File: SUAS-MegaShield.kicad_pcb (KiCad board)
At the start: 2 copper layers, 102.1 x 53.8 mm, 2 parts

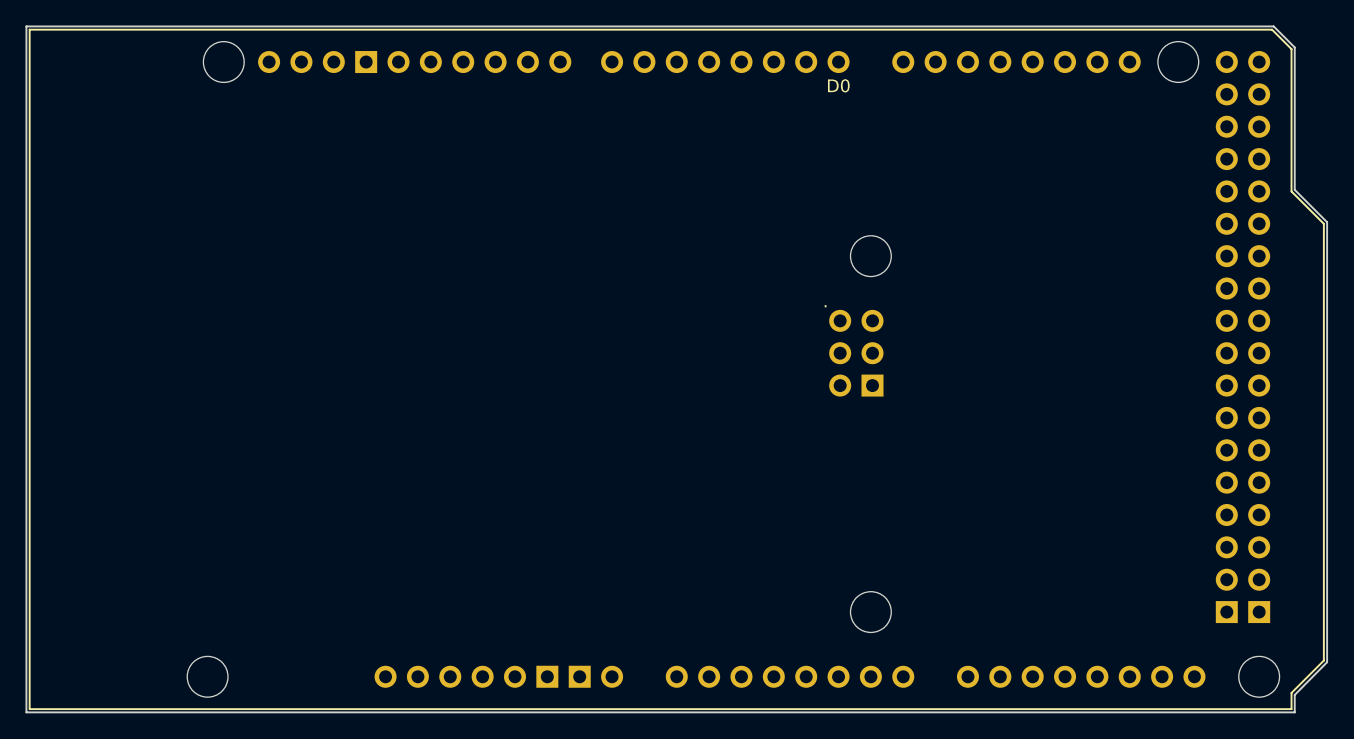
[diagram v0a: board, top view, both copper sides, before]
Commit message: Vcc trace width adjustment
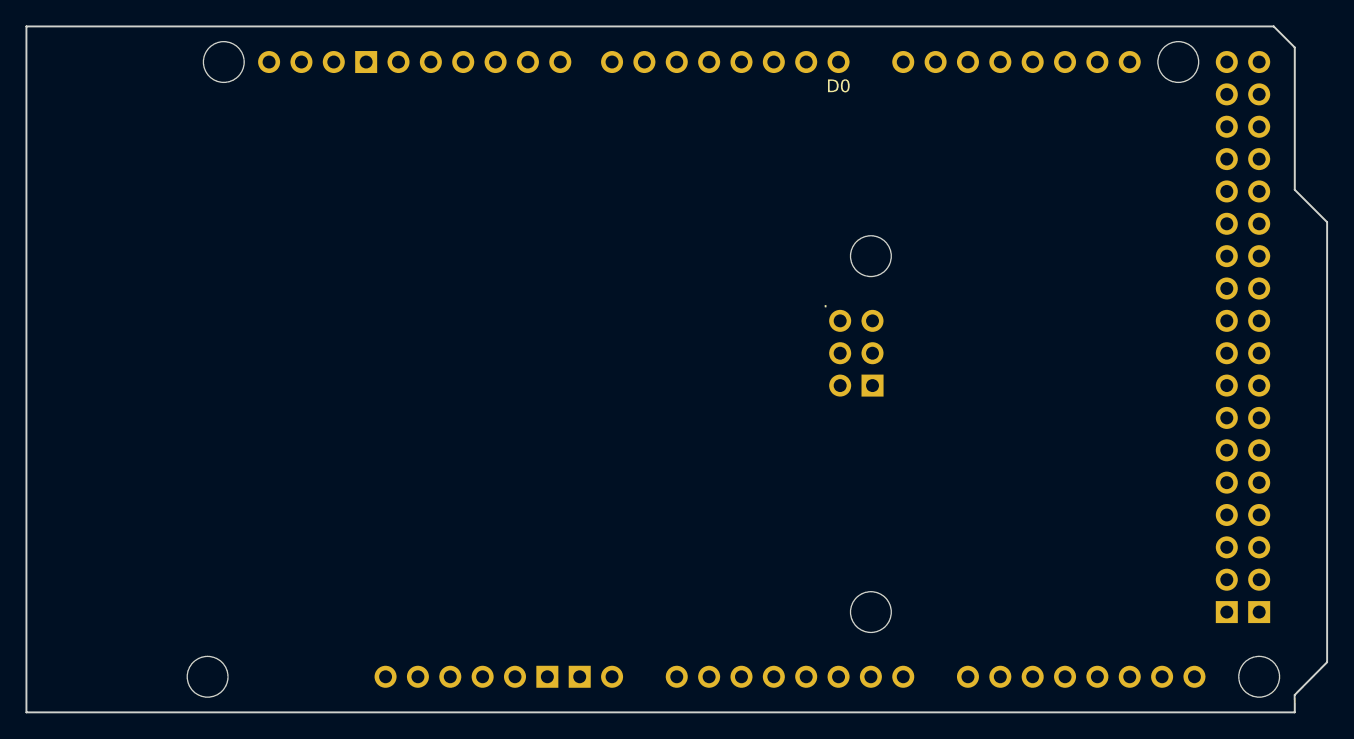
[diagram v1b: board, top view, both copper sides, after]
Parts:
- A1: value Arduino_Mega_Shield -> Arduino_Mega2560_R3_Shield; footprint arduino-library:Arduino_Giga_R1_WiFi_Shield -> arduino-library:Arduino_Mega2560_R3_Shield
